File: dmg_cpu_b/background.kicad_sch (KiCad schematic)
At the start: 64 parts

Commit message: BG and WIN sheets added.
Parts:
- added ACEN, ASUL, POVA: AND_2, symbol DMG_CPU_Cells:AND_2
- added AMUV, ASUM, COVE, COXO, DAHU, DODE, EVAD: TRI_INV_IF0, symbol DMG_CPU_Cells:TRI_INV_IF0
- added AXAD, BEJE, MOXE, PAHA, POHU: INVERTER_A, symbol DMG_CPU_Cells:INVERTER_A
- added BAFY: INVERTER_B, symbol DMG_CPU_Cells:INVERTER_B
- added NYZE, PUXA, ROGA, RUBU, RYKU: DFFR_B2, symbol DMG_CPU_Cells:DFFR_B2
- added PASO: NOR_2, symbol DMG_CPU_Cells:NOR_2
- added PECU: NAND_2, symbol DMG_CPU_Cells:NAND_2
- added RONE: NAND_4, symbol DMG_CPU_Cells:NAND_4
- added ROXY: NOR_LATCH, symbol DMG_CPU_Cells:NOR_LATCH
- added ROZE: NAND_3, symbol DMG_CPU_Cells:NAND_3
- added SOZU, SUHA, SYBY: XNOR, symbol DMG_CPU_Cells:XNOR
- gave numbers to parts that had none: 30
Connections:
- net FF43: no longer ANYP.1, BEDY.1
- net FF43_D0: now also SUHA.2 (1); no longer FAFO.4 (B), GAVE.5 (Q)
- net FF43_D1: now also SYBY.2 (1); no longer EMUX.5 (B), FYMO.5 (Q)
- net FF43_D2: now also SOZU.2 (1); no longer ECAB.5 (B), FEZU.5 (Q)
- net FF43_D3: no longer ETAM.5 (B), FUJO.5 (Q)
- net FF43_D4: no longer DEDE.5 (Q), DOTO.5 (B)
- net FF43_D5: no longer DABA.5 (B), FOTY.5 (Q)
- net FF43_D6: no longer EFYK.5 (B), FOHA.5 (Q)
- net FF43_D7: no longer EJOK.5 (B), FUNY.5 (Q)
- net H0: no longer FAFO.3 (A)
- net H1: no longer EMUX.4 (A)
- net H2: no longer ECAB.4 (A)
- net H3: no longer ETAM.4 (A)
- net H4: no longer DOTO.4 (A)
- net H5: no longer DABA.4 (A)
- net H6: no longer EFYK.4 (A)
- net H7: no longer EJOK.4 (A)
- net at AFEB.1 (~{ENA}), AJAN.1 (~{ENA}), ALEL.1 (~{ENA})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: now also CASE.1 (~{ENA}), CETA.1 (~{ENA}), CYPO.1 (~{ENA}), DAFE.1 (~{ENA}), DUHO.1 (~{ENA}), AMUV.1 (~{ENA}), BAFY.2, COVE.1 (~{ENA}), COXO.1 (~{ENA})
- net at ECAB.2 (SUM): now also DODE.2
- net at EMUX.2 (SUM): now also DAHU.2
- net at FAFO.2 (SUM): now also EVAD.2
- net MA0 renamed ~{MA0}
- net ~{MA0}: now also ASUM.3; no longer DUHO.3
- net MA1 renamed ~{MA1}
- net ~{MA1}: now also EVAD.3; no longer CASE.3
- net MA2 renamed ~{MA2}
- net ~{MA2}: now also DAHU.3; no longer CYPO.3
- net MA3 renamed ~{MA3}
- net ~{MA3}: now also DODE.3; no longer CETA.3
- net MA4 renamed ~{MA4}
- net ~{MA4}: no longer DAFE.3
- new net: ASUM.1 (~{ENA}), BEJE.2, DAHU.1 (~{ENA}), DODE.1 (~{ENA}), EVAD.1 (~{ENA})
- new net: RONE.2, SOZU.1
- new net: ROZE.1, RYKU.6 (Q), SOZU.3 (2)
- new net: PECU.3, RUBU.1 (CLK)
- new net: ACEN.2, ASUL.1, AXAD.2
- new net: ASUL.3, BEJE.1
- new net: RONE.1, ROXY.3 (Q)
- new net: RONE.3, SYBY.1
- new net: RONE.4, SUHA.1
- new net: POHU.1, RONE.5
- new net: ROGA.6 (Q), ROZE.2, SYBY.3 (2)
- new net: ROZE.3, RUBU.6 (Q), SUHA.3 (2)
- new net: PAHA.2, PASO.1, ROXY.1 (SET)
- new net: PASO.3, ROGA.2 (~{RESET}), ROGA.4 (~{RESET}), RUBU.2 (~{RESET}), RUBU.4 (~{RESET}), RYKU.2 (~{RESET}), RYKU.4 (~{RESET})
- new net: ACEN.3, BAFY.1
- new net: POHU.2, PUXA.3 (D)
- new net: NYZE.3 (D), POVA.2, PUXA.6 (Q)
- new net: ROGA.1 (CLK), RUBU.3 (D), RUBU.5 (~{Q})
- new net: NYZE.5 (~{Q}), POVA.1
- new net: ROGA.3 (D), ROGA.5 (~{Q}), RYKU.1 (CLK)
- new net: MOXE.2, NYZE.1 (CLK)
- new net: RYKU.3 (D), RYKU.5 (~{Q})
- new net +5V: COVE.2, COXO.2
- new net CLK2: MOXE.1
- new net FF40_D3: AMUV.2
- new net FF42: ANYP.1, BEDY.1
- new net FF42_D0: FAFO.4 (B), GAVE.5 (Q)
- new net FF42_D1: EMUX.5 (B), FYMO.5 (Q)
- new net FF42_D2: ECAB.5 (B), FEZU.5 (Q)
- new net FF42_D3: ETAM.5 (B), FUJO.5 (Q)
- new net FF42_D4: DEDE.5 (Q), DOTO.5 (B)
- new net FF42_D5: DABA.5 (B), FOTY.5 (Q)
- new net FF42_D6: EFYK.5 (B), FOHA.5 (Q)
- new net FF42_D7: EJOK.5 (B), FUNY.5 (Q)
- new net IN_WINDOW: AXAD.1
- new net MODE3: NYZE.2 (~{RESET}), NYZE.4 (~{RESET}), PAHA.1, PUXA.2 (~{RESET}), PUXA.4 (~{RESET})
- new net NETA: ASUL.2
- new net POTU: ACEN.1
- new net POVA: POVA.3, ROXY.4 (RESET)
- new net ROXO: PECU.1, PUXA.1 (CLK)
- new net ROZE: PECU.2, ROZE.4
- new net TEVO: PASO.2
- new net V0: FAFO.3 (A)
- new net V1: EMUX.4 (A)
- new net V2: ECAB.4 (A)
- new net V3: ETAM.4 (A)
- new net V4: DOTO.4 (A)
- new net V5: DABA.4 (A)
- new net V6: EFYK.4 (A)
- new net V7: EJOK.4 (A)
- new net XUHA: ASUM.2
- new net ~{MA10}: AMUV.3
- new net ~{MA11}: COVE.3
- new net ~{MA12}: COXO.3
- new net ~{MA5}: DUHO.3
- new net ~{MA6}: CASE.3
- new net ~{MA7}: CYPO.3
- new net ~{MA8}: CETA.3
- new net ~{MA9}: DAFE.3
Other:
- moved on the sheet: ABOD, ACUL, AFEB, AJAN, ALEL, ANYP, APYH, ARUR, ATAD, AVOG, AXEP, BABE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

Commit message: Some mistakes found in APU sheets, notes added for clarity. Edit in PPU sheets following review.
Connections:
- net FF42: now also ANYP.2, BEDY.2; no longer ANYP.1, BEDY.1
- net PPU_RD: now also ANYP.1; no longer ANYP.2
- net PPU_WR: now also BEDY.1; no longer BEDY.2
- net at SOZU.1: now also RONE.4; no longer RONE.2
- net at ROZE.1, SOZU.3 (2): now also RUBU.6 (Q); no longer RYKU.6 (Q)
- net at PECU.3: now also RYKU.1 (CLK); no longer RUBU.1 (CLK)
- net at SUHA.1: now also RONE.2; no longer RONE.4
- net at ROZE.3, SUHA.3 (2): now also RYKU.6 (Q); no longer RUBU.6 (Q)
- net at RUBU.3 (D), RUBU.5 (~{Q}): no longer ROGA.1 (CLK)
- net at ROGA.3 (D), ROGA.5 (~{Q}): now also RUBU.1 (CLK); no longer RYKU.1 (CLK)
- net at RYKU.3 (D), RYKU.5 (~{Q}): now also ROGA.1 (CLK)
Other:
- moved on the sheet: MOXE, NYZE, PAHA, PASO, PECU, POHU, POVA, PUXA, ROGA, RONE, ROXY, ROZE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

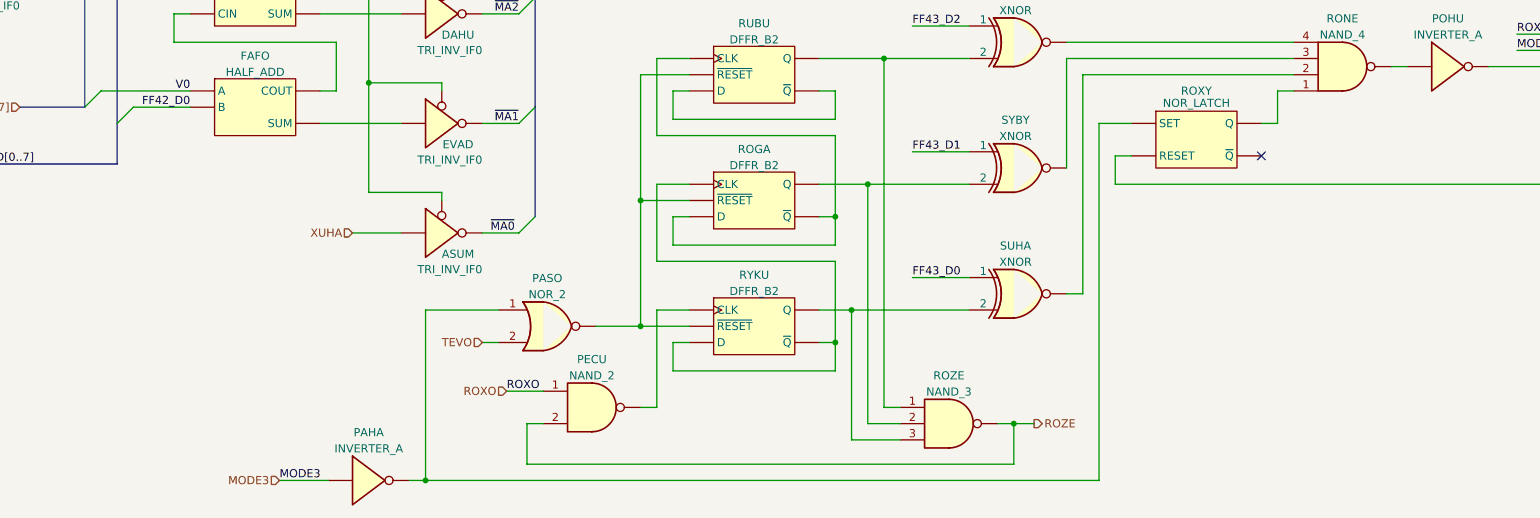
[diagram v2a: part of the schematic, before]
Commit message: VRAM interface sheet added but various edits in existing sheets. Notable merge of RESET, CLOCKS and FF04 DIV sheets
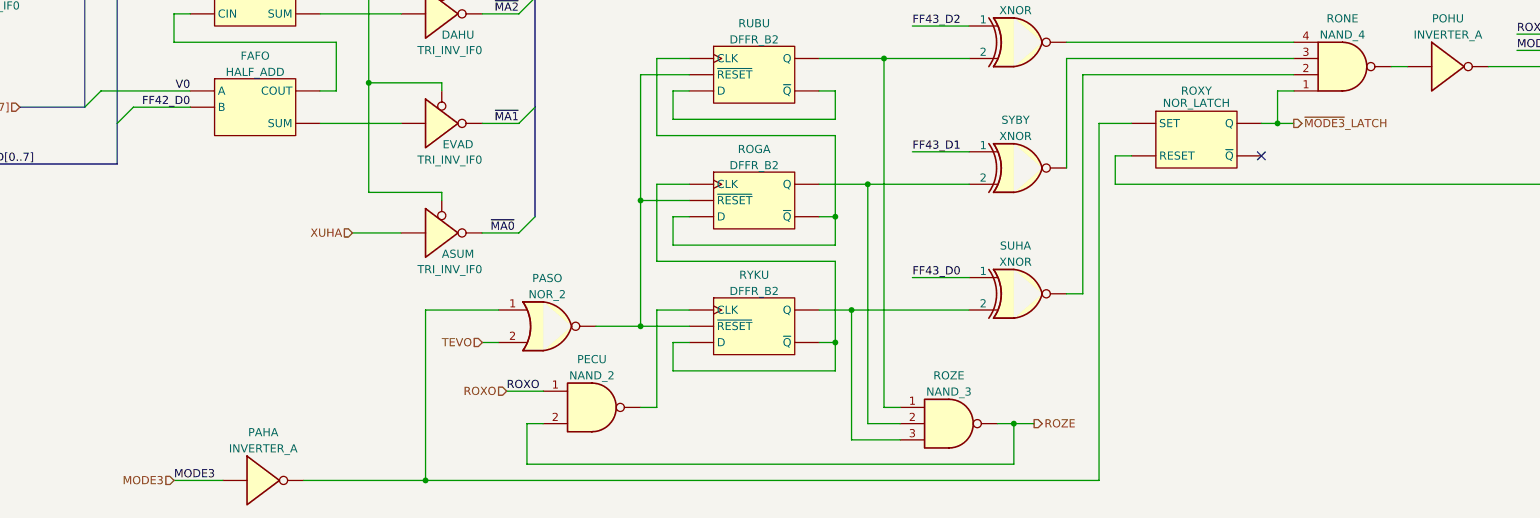
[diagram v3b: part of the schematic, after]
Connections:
- net ~{MODE3}_LATCH: now reaches RONE.1, ROXY.3 (Q)
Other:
- company: (none) -> CC-BY-SA-4.0 Régis Galland & Michael Singer -- Derived work from Furrtek
- title: (none) -> DMG CPU B
- moved on the sheet: PAHA
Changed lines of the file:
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@@
 (kicad_sch (version 20211123) (generator eeschema)
   (paper "A3")
+  (title_block
+    (title "DMG CPU B")
+    (date "2022-05-02")
+    (rev "0")
+    (company "CC-BY-SA-4.0 Régis Galland & Michael Singer -- Derived work from Furrtek")
+    (comment 1 "https://github.com/msinger/dmg-schematics")
+  )
   (junction (at 158.75 198.12) (diameter 0) (color 0 0 0 0)
   )
@@
   (junction (at 231.775 236.22) (diameter 0) (color 0 0 0 0)
   )
+  (junction (at 300.99 221.615) (diameter 0) (color 0 0 0 0)
+  )
   (junction (at 161.29 18.415) (diameter 0) (color 0 0 0 0)
   )
@@
     (stroke (width 0) (type default) (color 0 0 0 0))
   )
-  (wire (pts (xy 144.78 277.495) (xy 152.4 277.495))
+  (wire (pts (xy 128.27 277.495) (xy 135.89 277.495))
     (stroke (width 0) (type default) (color 0 0 0 0))
   )
@@
     (stroke (width 0) (type default) (color 0 0 0 0))
   )
+  (wire (pts (xy 300.99 221.615) (xy 303.53 221.615))
+    (stroke (width 0) (type default) (color 0 0 0 0))
+  )
   (wire (pts (xy 48.895 128.778) (xy 48.895 144.653))
     (stroke (width 0) (type default) (color 0 0 0 0))
@@
     (stroke (width 0) (type default) (color 0 0 0 0))
   )
-  (wire (pts (xy 165.1 277.495) (xy 167.64 277.495))
+  (wire (pts (xy 148.59 277.495) (xy 167.64 277.495))
     (stroke (width 0) (type default) (color 0 0 0 0))
   )
@@
     (effects (font (size 1.27 1.27)) (justify right bottom))
   )
-  (label "MODE3" (at 144.78 277.495 0)
+  (label "MODE3" (at 128.27 277.495 0)
     (effects (font (size 1.27 1.27)) (justify left bottom))
   )
@@
     (effects (font (size 1.27 1.27)) (justify right))
   )
-  (hierarchical_label "MODE3" (shape input) (at 144.78 277.495 180)
+  (hierarchical_label "~{MODE3}_LATCH" (shape output) (at 303.53 221.615 0)
+    (effects (font (size 1.27 1.27)) (justify left))
+  )
+  (hierarchical_label "MODE3" (shape input) (at 128.27 277.495 180)
     (effects (font (size 1.27 1.27)) (justify right))
   )
@@
     (pin "6")
   )
-  (symbol (lib_id "DMG_CPU_Cells:INVERTER_A") (at 158.75 277.495 0) (unit 1)
+  (symbol (lib_id "DMG_CPU_Cells:INVERTER_A") (at 142.24 277.495 0) (unit 1)
     (in_bom yes) (on_board yes)
-    (property "Reference" "PAHA" (id 0) (at 158.75 269.9852 0))
-    (property "Value" "INVERTER_A" (id 1) (at 158.75 272.5221 0))
-    (property "Footprint" "" (id 2) (at 156.21 277.495 0)
+    (property "Reference" "PAHA" (id 0) (at 142.24 269.9852 0))
+    (property "Value" "INVERTER_A" (id 1) (at 142.24 272.5221 0))
+    (property "Footprint" "" (id 2) (at 139.7 277.495 0)
       (effects (font (size 1.27 1.27)) hide)
     )
-    (property "Datasheet" "http://iceboy.a-singer.de/doc/dmg_cells.html#inv_a" (id 3) (at 160.02 285.115 0)
+    (property "Datasheet" "http://iceboy.a-singer.de/doc/dmg_cells.html#inv_a" (id 3) (at 143.51 285.115 0)
       (effects (font (size 1.27 1.27)) hide)
     )

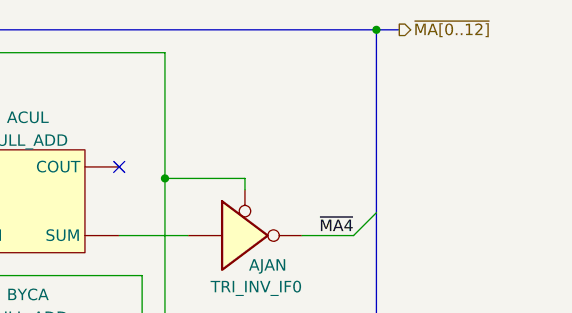
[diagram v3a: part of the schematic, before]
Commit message: bg and sp px shifters added.
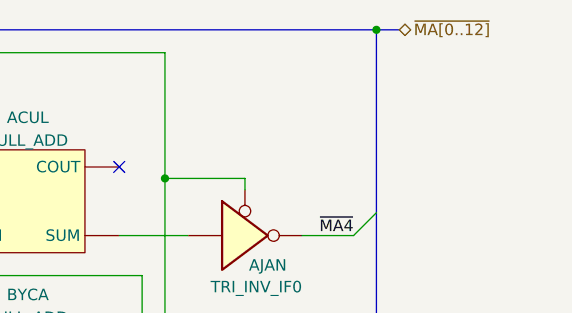
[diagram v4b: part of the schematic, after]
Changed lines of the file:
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@@
     (effects (font (size 1.27 1.27)) (justify right))
   )
-  (hierarchical_label "~{MA[0..12]}" (shape output) (at 393.7 15.875 0)
+  (hierarchical_label "~{MA[0..12]}" (shape tri_state) (at 393.7 15.875 0)
     (effects (font (size 1.27 1.27)) (justify left))
   )

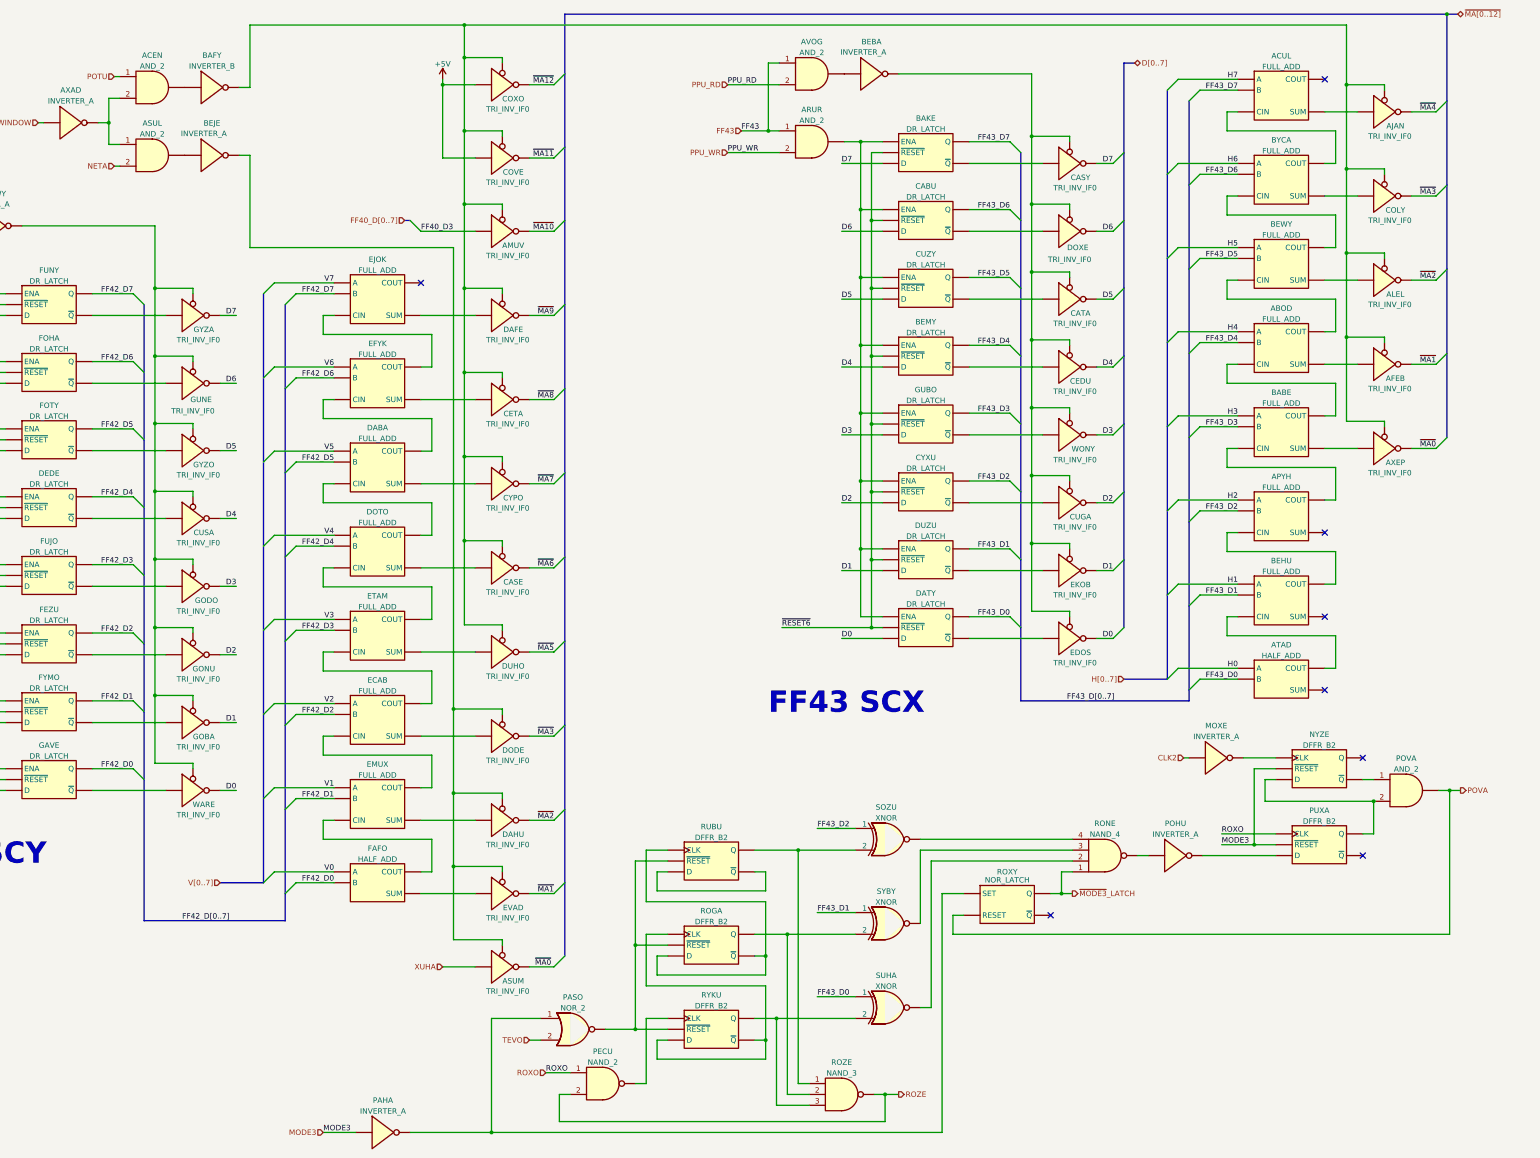
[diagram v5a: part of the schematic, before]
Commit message: New sheet created to free up space on LCD and SCX/SCY sheets and joined common signals.
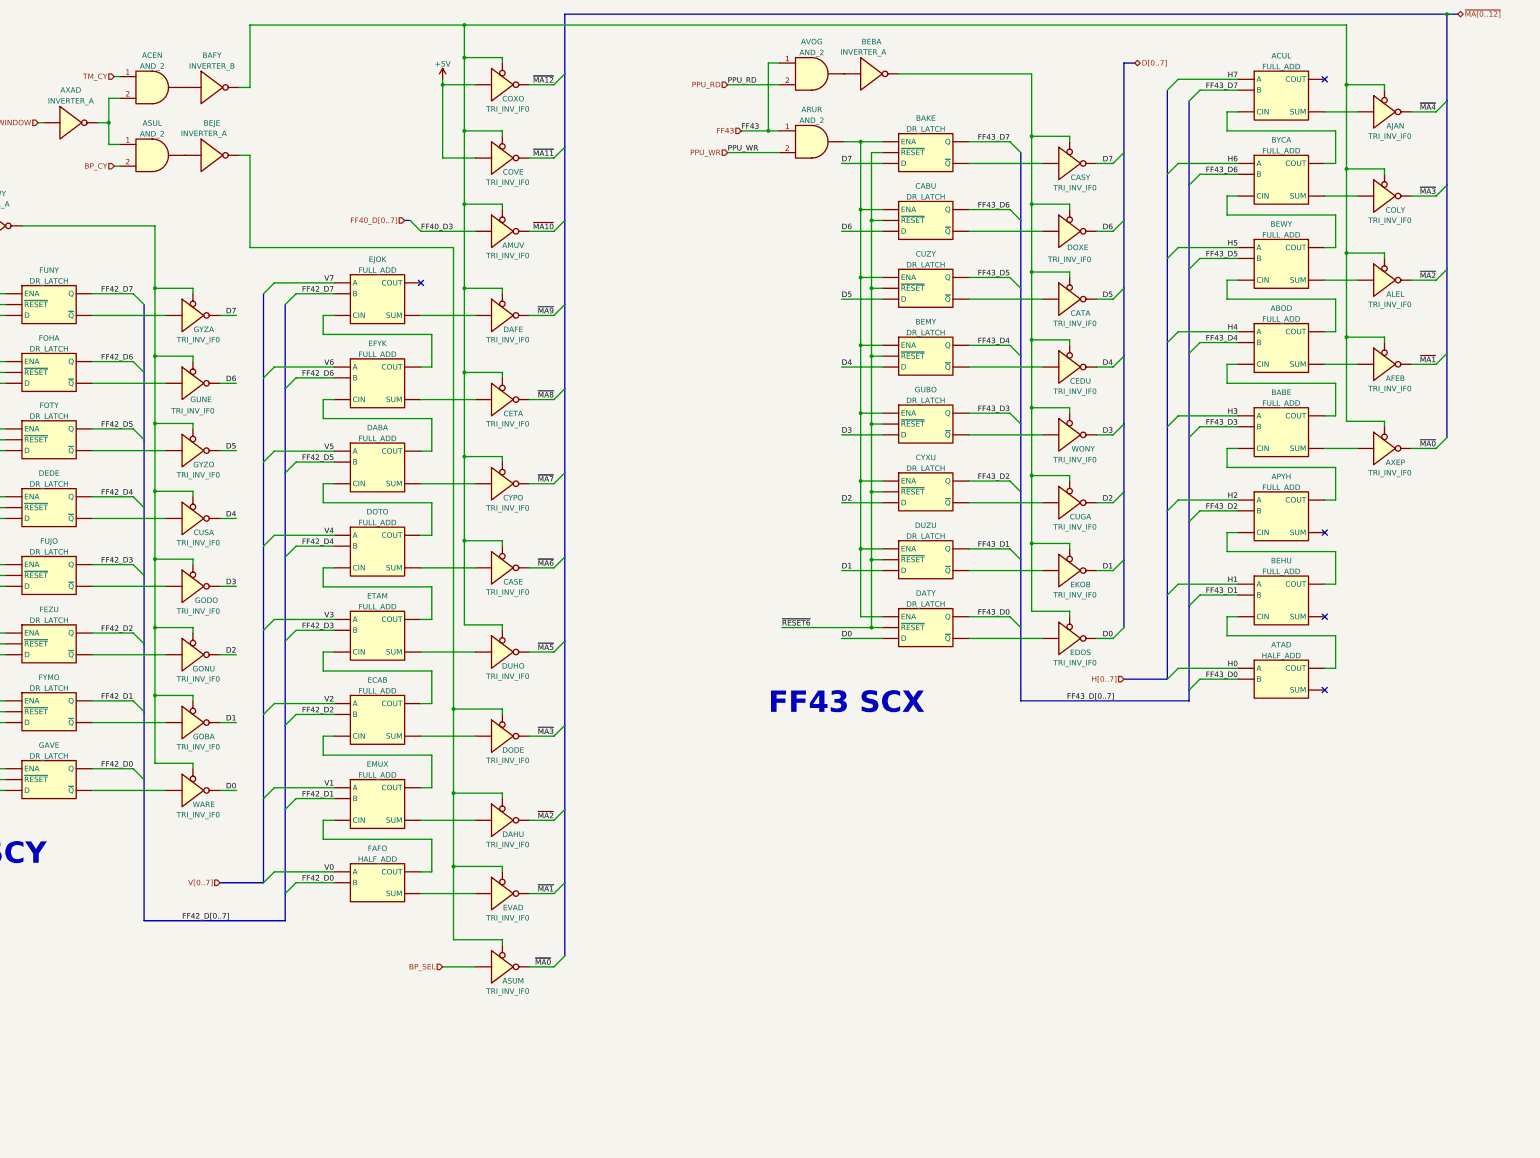
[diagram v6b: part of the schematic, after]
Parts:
- removed MOXE, PAHA, POHU: INVERTER_A, symbol DMG_CPU_Cells:INVERTER_A
- removed NYZE, PUXA, ROGA, RUBU, RYKU: DFFR_B2, symbol DMG_CPU_Cells:DFFR_B2
- removed PASO: NOR_2, symbol DMG_CPU_Cells:NOR_2
- removed PECU: NAND_2, symbol DMG_CPU_Cells:NAND_2
- removed POVA: AND_2, symbol DMG_CPU_Cells:AND_2
- removed RONE: NAND_4, symbol DMG_CPU_Cells:NAND_4
- removed ROXY: NOR_LATCH, symbol DMG_CPU_Cells:NOR_LATCH
- removed ROZE: NAND_3, symbol DMG_CPU_Cells:NAND_3
- removed SOZU, SUHA, SYBY: XNOR, symbol DMG_CPU_Cells:XNOR
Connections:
- net NETA renamed BP_CY
- net POTU renamed TM_CY
- net XUHA renamed BP_SEL
- no-connect marks 8 -> 5
